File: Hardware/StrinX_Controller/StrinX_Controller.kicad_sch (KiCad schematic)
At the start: 0 parts

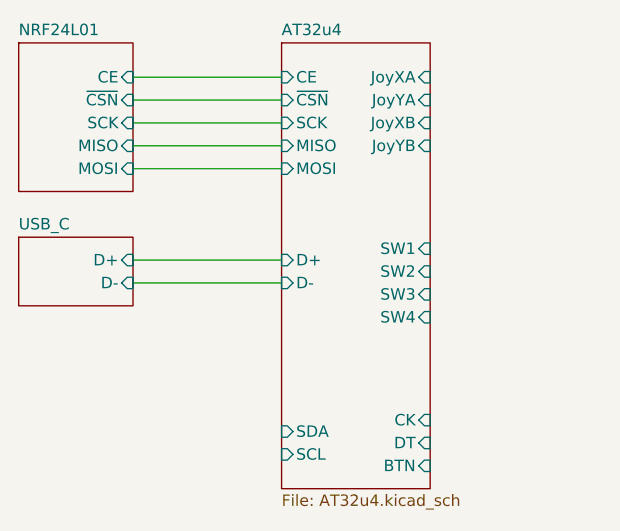
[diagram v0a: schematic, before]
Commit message: Add device and footprint
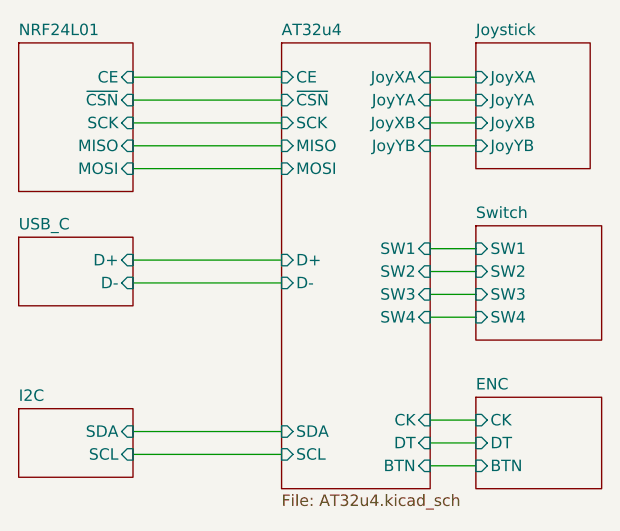
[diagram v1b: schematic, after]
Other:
- added sheet ENC (ENC.kicad_sch)
- added sheet I2C (I2C.kicad_sch)
- added sheet Joystick (Joystick.kicad_sch)
- added sheet Switch (Switch.kicad_sch)
